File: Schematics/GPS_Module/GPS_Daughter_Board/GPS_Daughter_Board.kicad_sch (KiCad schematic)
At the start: 17 parts, among them J4 25SH-B-06-TR, U3 SAM-M10Q, U8 LM66100DCKR

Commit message: starting daughter board PCB layout
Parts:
- removed J4: 25SH-B-06-TR, Connector_PinHeader_2.54mm:PinHeader_1x06_P2.54mm_Horizontal, symbol Connector:Conn_01x06_Socket
- added J1: 470804001, footprints:CONN_47080-4001_MOL_SATA, symbol CONN_47080-4001_MOL_SATA:470804001
- C22: footprint Capacitor_THT:CP_Radial_D12.5mm_P7.50mm -> CB5R5334HF-ZJP:CB5R5334HF-ZJP
- U8: footprint LMR66100:SC-70-6 -> LMR66100:SC-70-6_Handsoldering
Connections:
- net EXTINT_GPS_D: now also J1.3
- net GPS_3.3V: now also J1.2
- net GPS_GND: now also J1.1
- net PPS_GPS_D: now also J1.7
- net RST_GPS_D: now also J1.4
- net SCL_GPS_D: now also J1.6
- net SDA_GPS_D: now also J1.5
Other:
- note added: "External GPS Antenna Board Connector"
- note added: "Vf=2.3V, I=1.8mA, R=560"
- note removed: "JST connect (on daughter)"
- note removed: "NEED PROPER FOOTPRINT FOR JST CONNECTOR (change to SMD)"

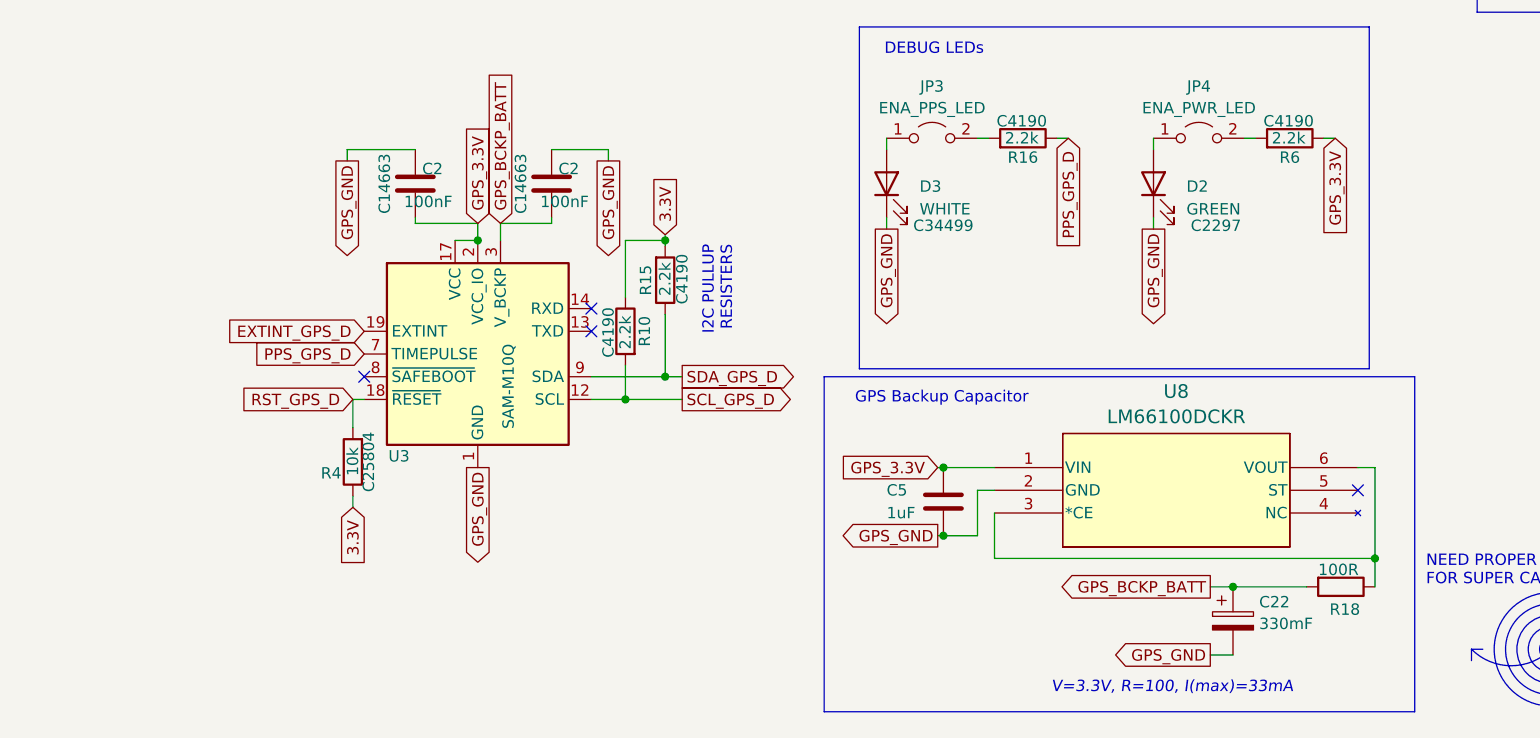
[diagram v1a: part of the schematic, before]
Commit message: finished daughter board waiting for approval
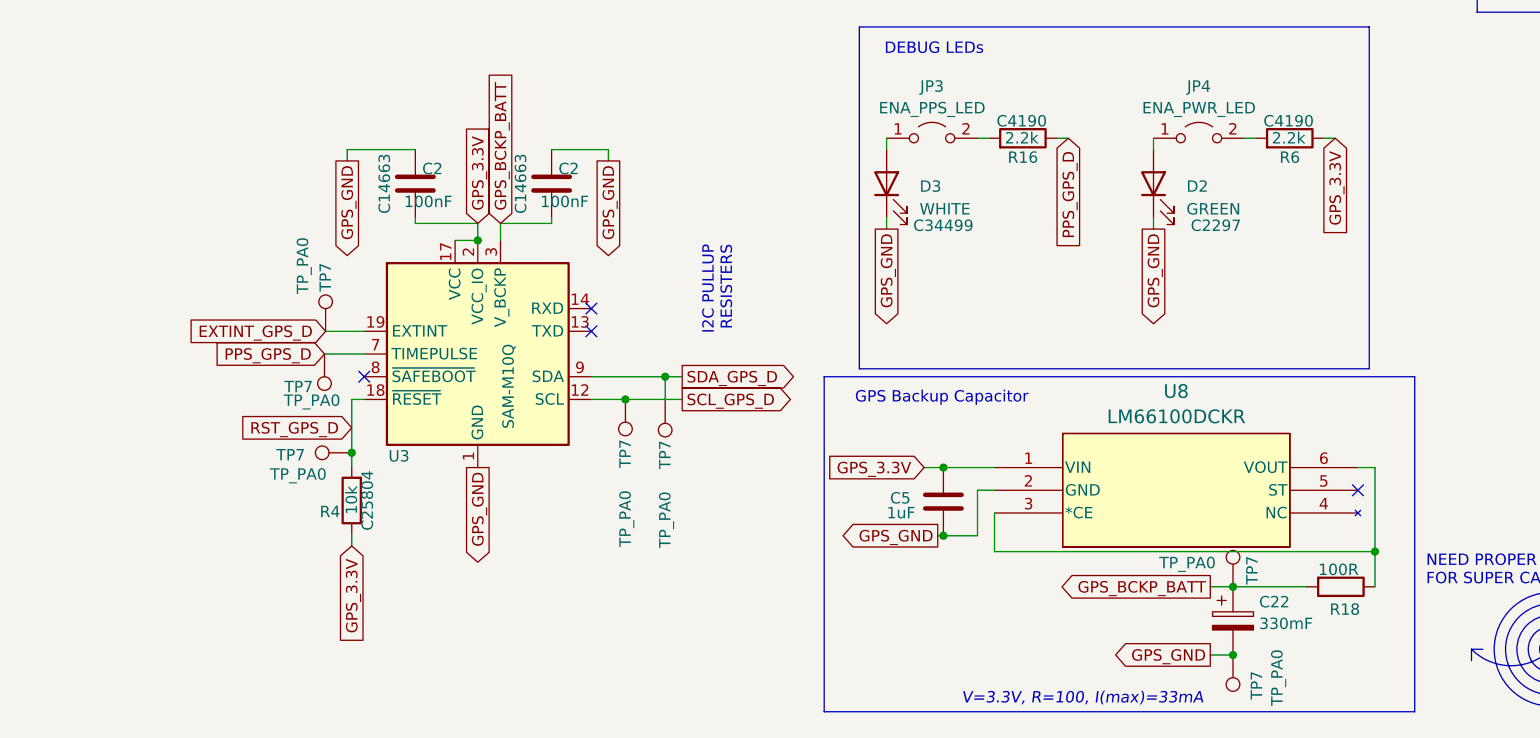
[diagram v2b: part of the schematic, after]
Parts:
- removed R10, R15: 2.2k, Resistor_SMD:R_0603_1608Metric, symbol Device:R
- added TP7 (x7): TP_PA0, TestPoint:TestPoint_Pad_1.5x1.5mm, symbol Connector:TestPoint
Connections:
- net 3.3V is gone; now on net GPS_3.3V: R4.1
- net EXTINT_GPS_D: now also TP7.1
- net GPS_BCKP_BATT: now also TP7.1
- net GPS_GND: now also TP7.1
- net PPS_GPS_D: now also TP7.1
- net RST_GPS_D: now also TP7.1
- net SCL_GPS_D: now also TP7.1
- net SDA_GPS_D: now also TP7.1
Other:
- moved on the sheet: R4

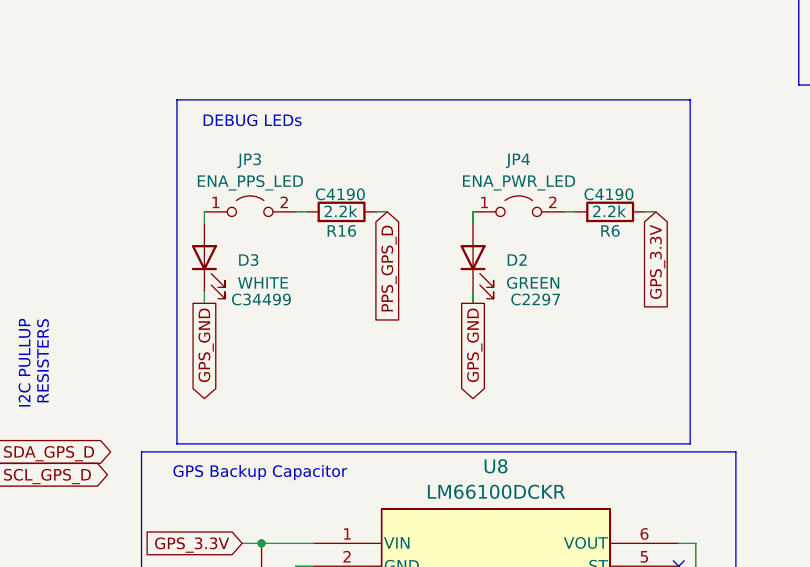
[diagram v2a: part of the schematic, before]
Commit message: checking lcsc and digikey numbers
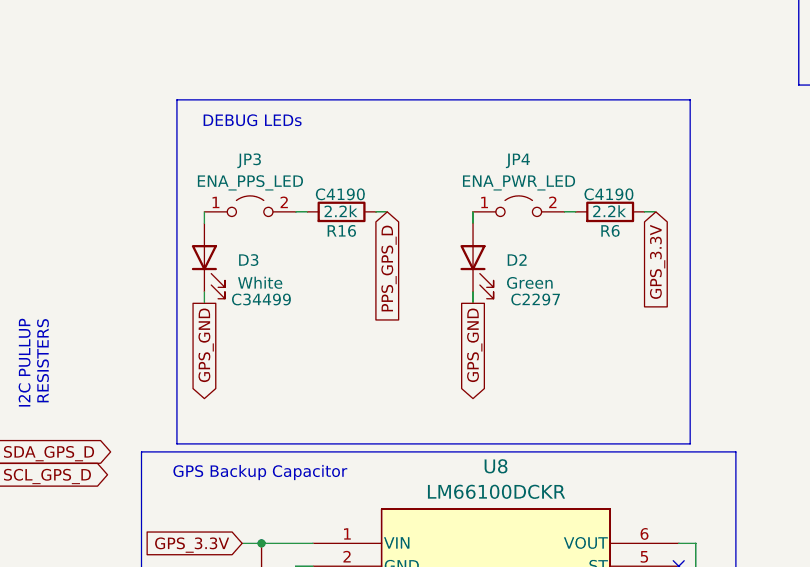
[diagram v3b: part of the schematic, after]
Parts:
- D2: value GREEN -> Green
- D3: value WHITE -> White
- U3: Digikey (none) -> 672-SAM-M10Q-00BCT-ND
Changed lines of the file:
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@@
       (effects (font (size 1.27 1.27)) (justify right))
     )
-    (property "Value" "GREEN" (at 158.115 82.4865 90)
+    (property "Value" "Green" (at 158.115 82.4865 90)
       (effects (font (size 1.27 1.27)) (justify right))
     )
@@
       (effects (font (size 1.27 1.27)) (justify right))
     )
-    (property "Value" "WHITE" (at 128.27 82.4865 90)
+    (property "Value" "White" (at 128.27 82.4865 90)
       (effects (font (size 1.27 1.27)) (justify right))
     )
@@
       (effects (font (size 1.27 1.27)) hide)
     )
+    (property "Digikey" "672-SAM-M10Q-00BCT-ND" (at 78.867 98.679 0)
+      (effects (font (size 1.27 1.27)) hide)
+    )
